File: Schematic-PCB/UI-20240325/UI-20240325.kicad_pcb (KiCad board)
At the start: 2 copper layers, 65.5 x 30.7 mm, 20 parts, among them J1 Conn_01x10_Pin, SW1 SW_Push, SW2 SW_Push, SW3 SW_Push, SW4 SW_Push, SW5 SW_Push

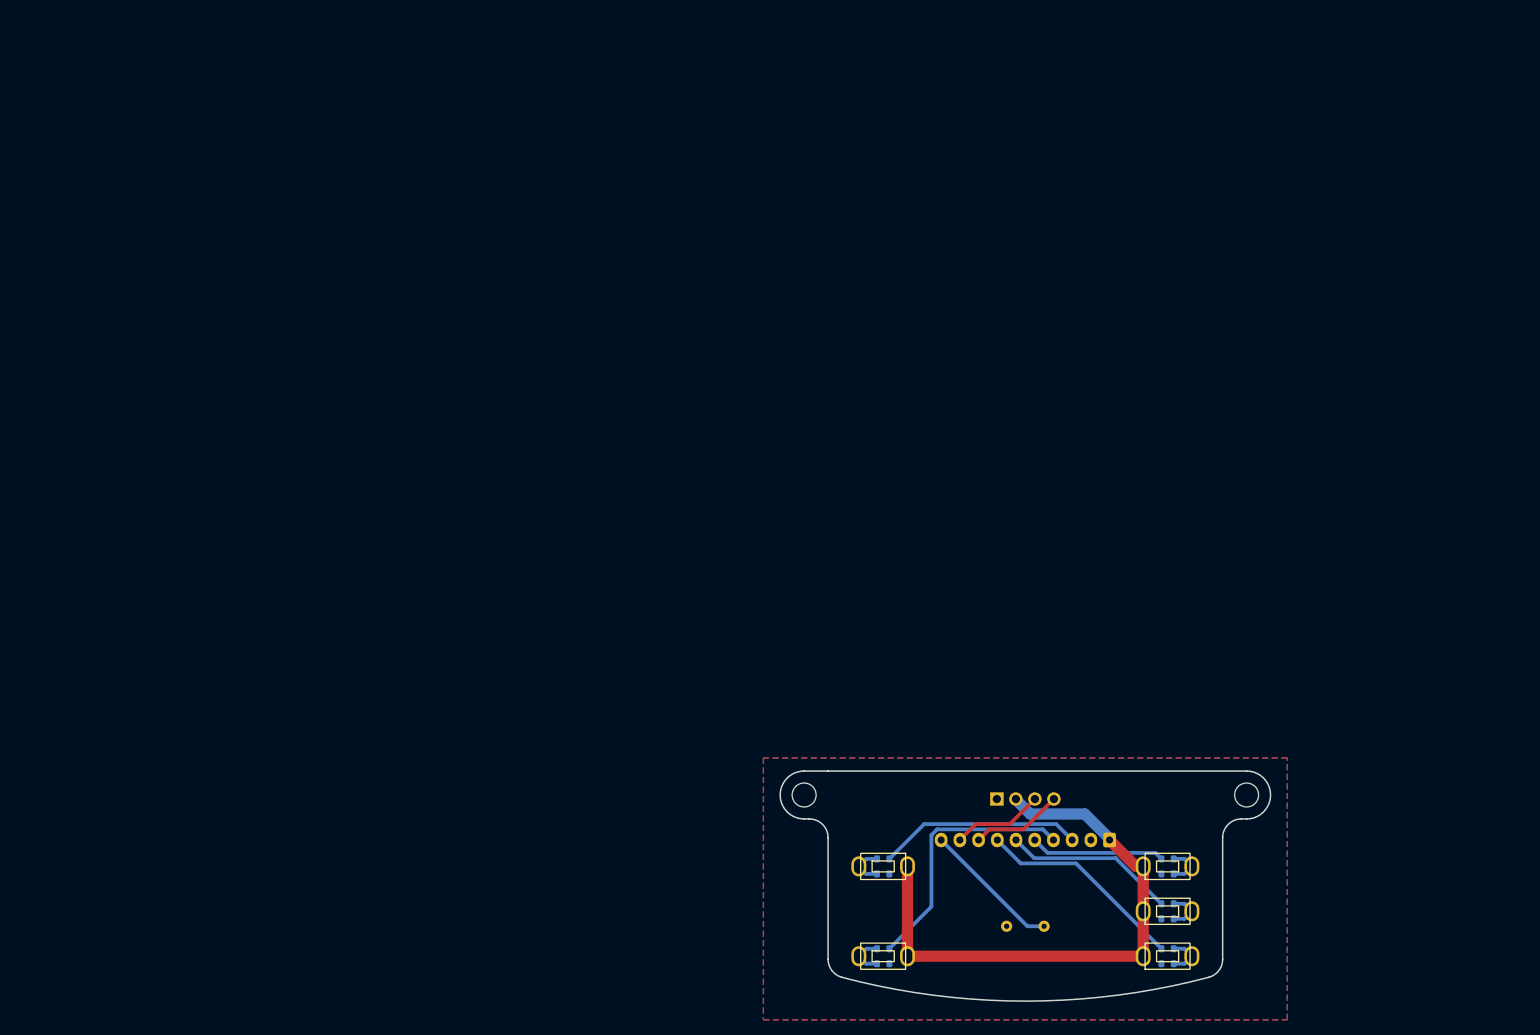
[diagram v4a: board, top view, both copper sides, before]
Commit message: UI基板の配線がねじれてしまう問題を解決した
ピンアサインに変更有、ピンアサイン図の変更が必要
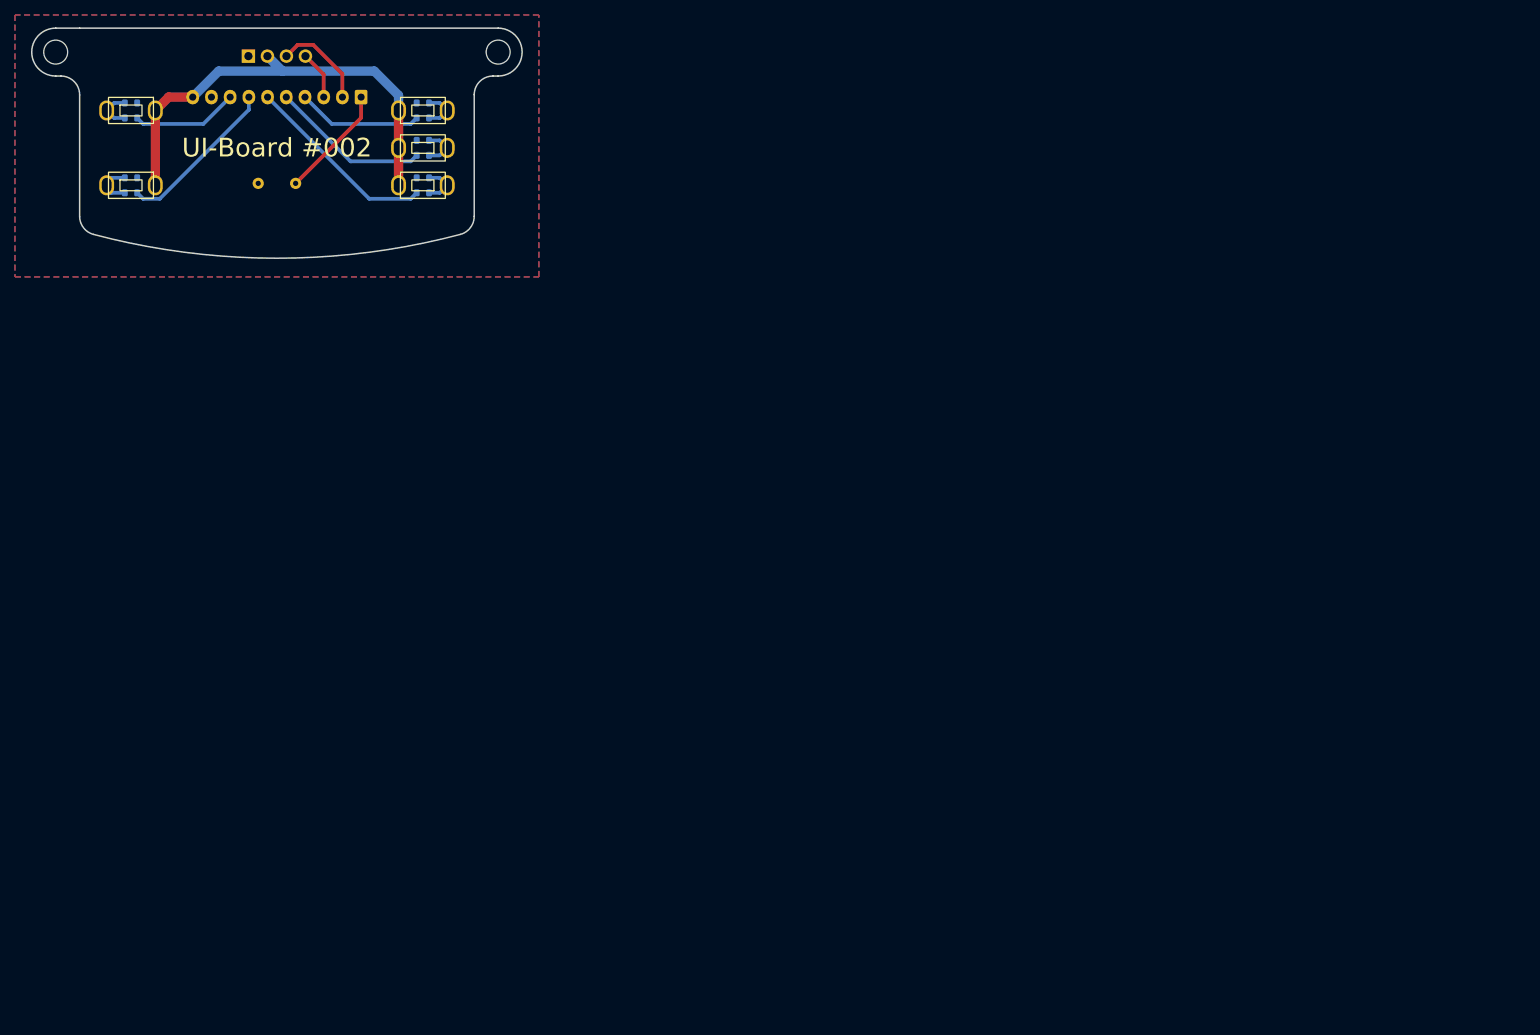
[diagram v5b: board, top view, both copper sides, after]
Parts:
- BZ1: footprint @2024-UI:PKM13EPYH4000-A0 -> @2024TOINIOT2-UI:PKM13EPYH4000-A0
- R5: value 1K -> 500
- SW1, SW2, SW3, SW4, SW5: footprint @2024-UI:TVBP06-B043C -> @2024TOINIOT2-UI:TVBP06-B043C
- U1: footprint @2024-UI:Display -> @2024TOINIOT2-UI:Display
- moved R7 145.3 mm to (-19.5, 20.0)
- moved R10 144.7 mm to (19.5, 20.0)
- moved R9 143.9 mm to (19.5, 15.0)
- moved R6 143.9 mm to (-19.5, 10.0)
- moved SW2 143.9 mm to (-19.5, 21.0)
- moved R8 143.2 mm to (19.5, 10.0)
- moved SW5 143.2 mm to (19.5, 21.0)
- moved SW4 142.5 mm to (19.5, 16.0)
- moved R2 142.5 mm to (-19.5, 22.0)
- moved SW1 142.5 mm to (-19.5, 11.0)
- moved R5 141.8 mm to (19.5, 22.0)
- moved SW3 141.8 mm to (19.5, 11.0)
- moved R1 141.1 mm to (-19.5, 12.0)
- moved R4 141.1 mm to (19.5, 17.0)
- moved REF** 140.9 mm to (29.6, 3.20)
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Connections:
- J1 pad 1: +3.3V -> BUZZER
- J1 pad 10: BUZZER -> +3.3V
- J1 pad 2: GND -> SCL
- J1 pad 3: SW-TAC-1 -> SDA
- J1 pad 4: SW-TAC-2 -> SW-TAC-3
- J1 pad 5: SW-TAC-3 -> SW-TAC-4
- J1 pad 6: SW-TAC-4 -> SW-TAC-5
- J1 pad 7: SW-TAC-5 -> SW-TAC-2
- J1 pad 8: SDA -> SW-TAC-1
- J1 pad 9: SCL -> GND
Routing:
- net +3.3V: track 76.4 -> 60.9 mm
- net SW-TAC-1: track 27.2 -> 14.2 mm
- net SW-TAC-2: track 34.7 -> 21.9 mm
- net SDA: track 12.3 -> 6.49 mm
- net BUZZER: track 18.5 -> 15.1 mm
- net SW-TAC-5: track 27.9 -> 25.9 mm
- net SW-TAC-4: track 23.0 -> 21.3 mm
- net SW-TAC-3: track 18.0 -> 16.7 mm
- net Net-(R2-Pad2): track 5.68 -> 6.48 mm
- net SCL: track 12.3 -> 12.8 mm
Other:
- board text added: "UI-Board #002"

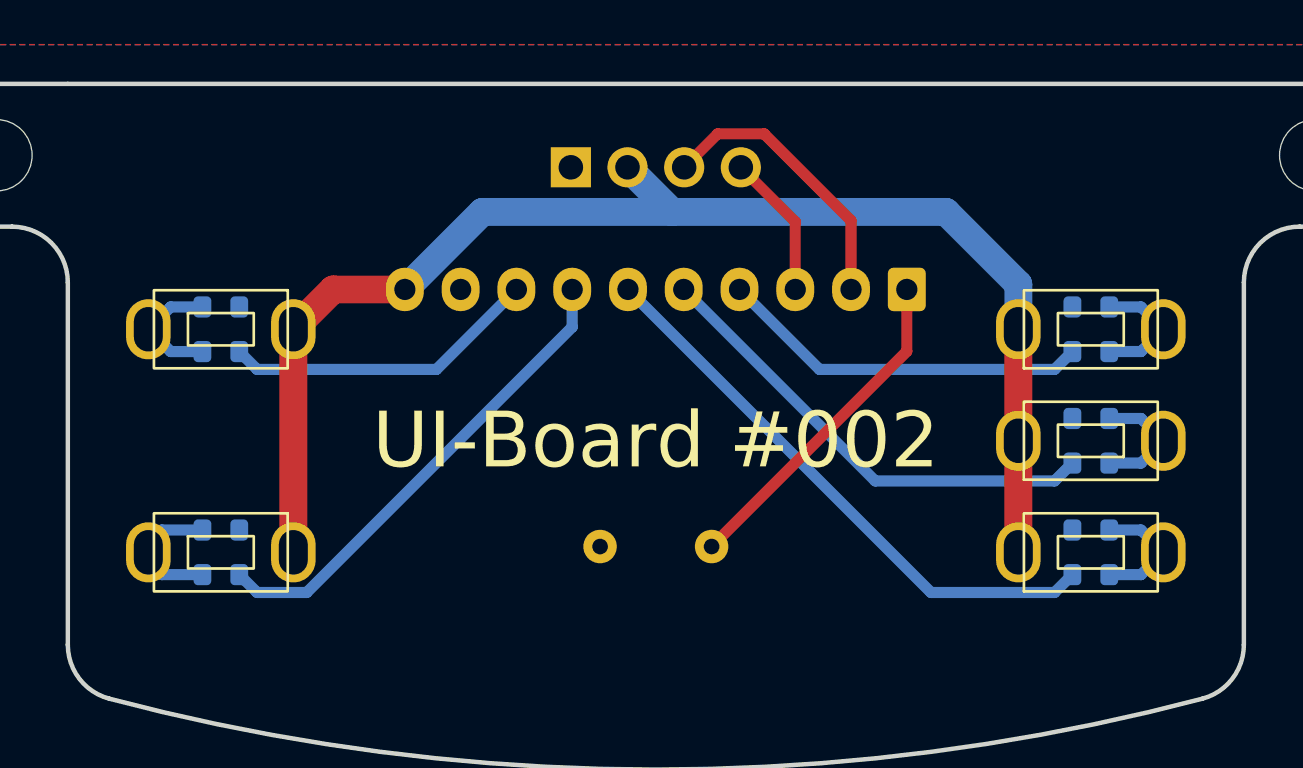
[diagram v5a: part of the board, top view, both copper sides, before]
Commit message: UI基板を修正/MD基板を修正/メイン基板を作り直し （ver.002）
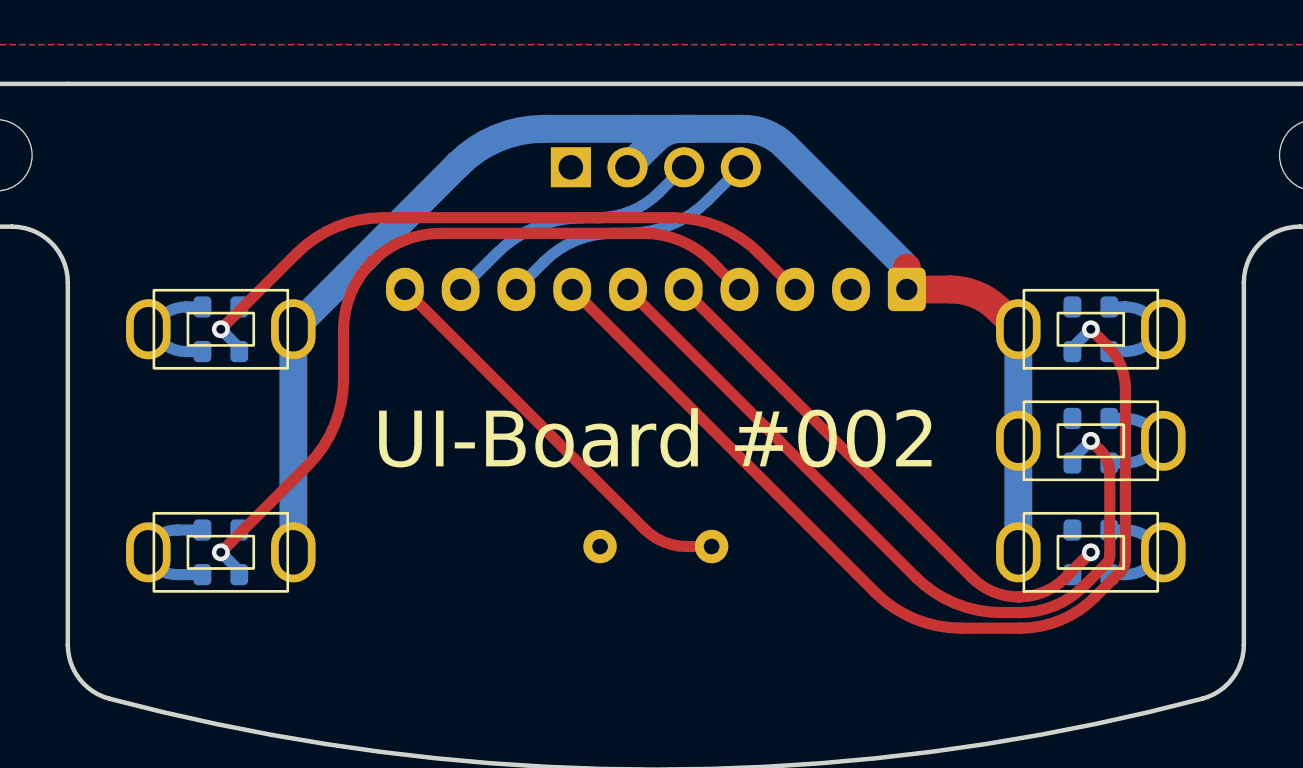
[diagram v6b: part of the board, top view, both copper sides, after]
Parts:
- R1, R2, R3, R4: value 1K -> 500
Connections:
- J1 pad 1: BUZZER -> +3.3V
- J1 pad 10: +3.3V -> BUZZER
- J1 pad 2: SCL -> GND
- J1 pad 3: SDA -> SW-TAC-1
- J1 pad 4: SW-TAC-3 -> SW-TAC-2
- J1 pad 5: SW-TAC-4 -> SW-TAC-5
- J1 pad 6: SW-TAC-5 -> SW-TAC-4
- J1 pad 7: SW-TAC-2 -> SW-TAC-3
- J1 pad 8: SW-TAC-1 -> SDA
- J1 pad 9: GND -> SCL
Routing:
- net SW-TAC-3: track 16.7 -> 44.2 mm, vias 0 -> 1
- net SW-TAC-1: track 14.2 -> 30.0 mm, vias 0 -> 1
- net SW-TAC-4: track 21.3 -> 35.1 mm, vias 0 -> 1
- net SW-TAC-2: track 21.9 -> 34.3 mm, vias 0 -> 1
- net SDA: track 6.49 -> 11.9 mm
- net BUZZER: track 15.1 -> 18.4 mm
- net +3.3V: track 60.9 -> 63.3 mm
- net SCL: track 12.8 -> 11.8 mm
- net SW-TAC-5: track 25.9 -> 25.8 mm, vias 0 -> 1

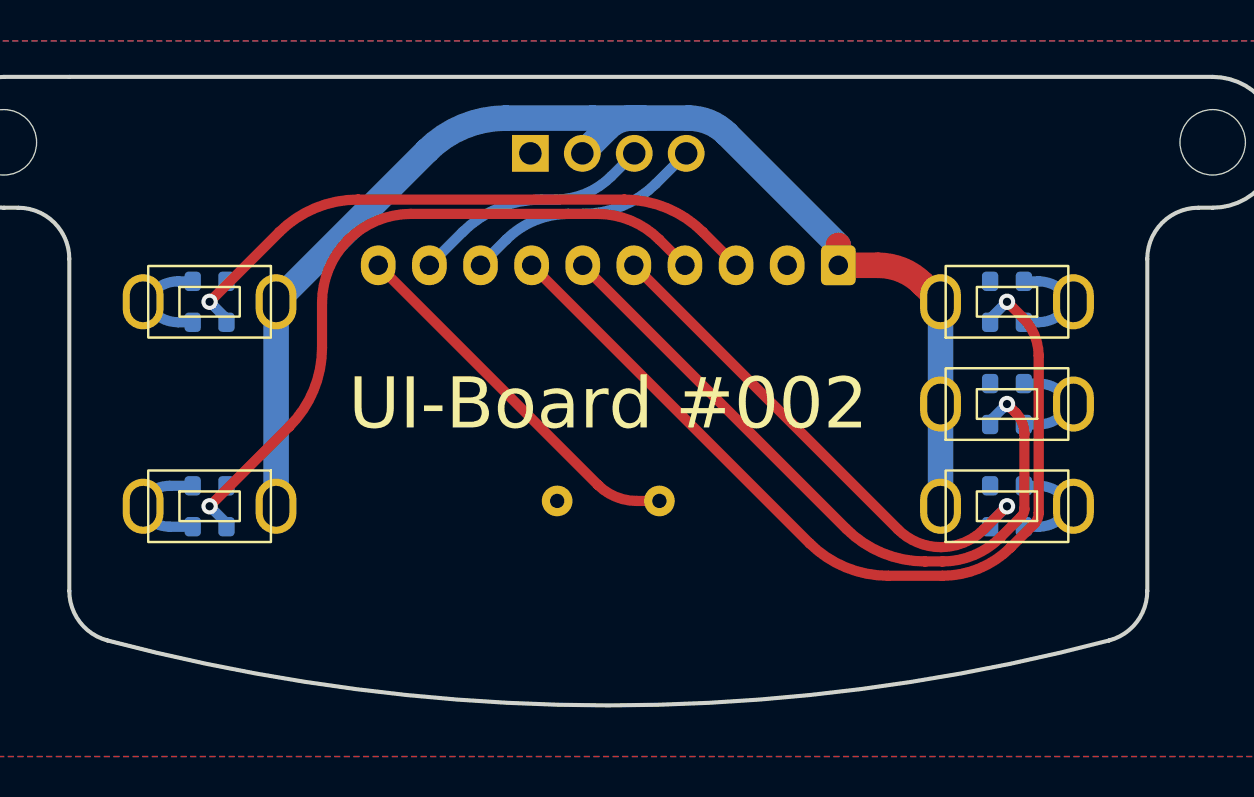
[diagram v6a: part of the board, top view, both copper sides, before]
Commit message: update: UI基板の更新など
発注用ファイルの出力・UI基板の仕様変更
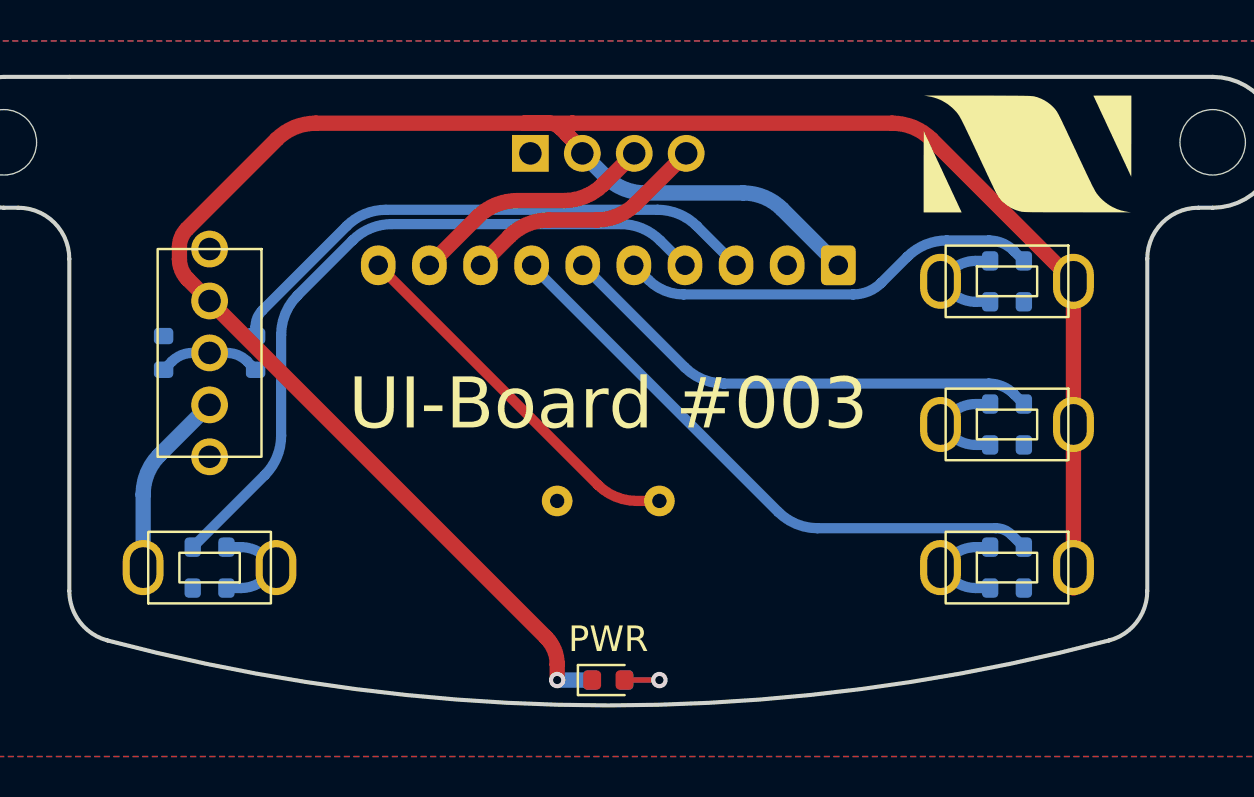
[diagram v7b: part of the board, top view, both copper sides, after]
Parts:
- added D1: PWR, LED_SMD:LED_0603_1608Metric, F.Cu at (0.00, 29.5)
- added R11: 10K, Resistor_SMD:R_0603_1608Metric, B.Cu at (19.5, 25.0)
- J1: value Conn_01x10_Pin -> Conn
- R1, R3, R5: value 500 -> 1K
- R10: value 10K -> 330
- R2, R4: value 500 -> 10K
- R7, R9: value 10K -> 1K
- SW1: value SW_Push -> SW_SPDT; footprint @2024TOINIOT2-UI:TVBP06-B043C -> @2024TOINIOT2-UI:2MS1-T1-B4-VS2-Q-E-S
- moved R3 40.5 mm to (-19.5, 23.0)
- moved R4 39.8 mm to (-19.5, 25.0)
- moved R7 39.2 mm to (19.5, 16.0)
- moved R6 39.0 mm to (19.5, 11.0)
- moved R10 21.7 mm to (0.00, 29.5)
- moved R5 13.0 mm to (19.5, 9.00), turned to 180 degrees
- moved R2 8.79 mm to (-21.8, 13.5), turned to -90 degrees
- moved R8 8.00 mm to (19.5, 18.0), turned to 180 degrees
- moved R9 8.00 mm to (19.5, 23.0), turned to 180 degrees
- moved SW2 3.00 mm to (-19.5, 24.0), turned to 180 degrees
- moved SW5 3.00 mm to (19.5, 24.0), turned to 0 degrees
- moved R1 2.70 mm to (-17.2, 13.5), turned to -90 degrees
- moved SW1 2.50 mm to (-19.5, 13.5), turned to -90 degrees
- moved SW3 1.00 mm to (19.5, 10.0), turned to 0 degrees
- moved SW4 1.00 mm to (19.5, 17.0), turned to 0 degrees
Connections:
- J1 pad 5: SW-TAC-5 -> SW-TAC-3
- J1 pad 7: SW-TAC-3 -> SW-TAC-5
- R1 pad 2: Net-(R1-Pad2) -> Net-(SW1-B)
- R10 pad 1: GND -> +3.3V
- R10 pad 2: Net-(R10-Pad2) -> Net-(D1-A)
- R2 pad 1: SW-TAC-2 -> GND
- R2 pad 2: Net-(R2-Pad2) -> Net-(SW1-B)
- R3 pad 1: SW-TAC-3 -> SW-TAC-2
- R4 pad 1: SW-TAC-4 -> GND
- R4 pad 2: Net-(R4-Pad2) -> Net-(R3-Pad2)
- R5 pad 1: SW-TAC-5 -> SW-TAC-3
- R5 pad 2: Net-(R10-Pad2) -> Net-(R5-Pad2)
- R6 pad 2: Net-(R1-Pad2) -> Net-(R5-Pad2)
- R7 pad 1: GND -> SW-TAC-4
- R7 pad 2: Net-(R2-Pad2) -> Net-(R7-Pad2)
- R8 pad 2: Net-(R3-Pad2) -> Net-(R7-Pad2)
- R9 pad 1: GND -> SW-TAC-5
- R9 pad 2: Net-(R4-Pad2) -> Net-(R11-Pad2)
- SW1 pad 1: Net-(R1-Pad2) -> +3.3V
- SW1 pad 2: +3.3V -> Net-(SW1-B)
- SW2 pad 1: Net-(R2-Pad2) -> Net-(R3-Pad2)
- SW3 pad 1: Net-(R3-Pad2) -> Net-(R5-Pad2)
- SW4 pad 1: Net-(R4-Pad2) -> Net-(R7-Pad2)
- SW5 pad 1: Net-(R10-Pad2) -> Net-(R11-Pad2)
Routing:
- net +3.3V: track 63.3 -> 123.7 mm, vias 0 -> 1
- net SW-TAC-3: track 44.2 -> 20.7 mm, vias 1 -> 0
- net SW-TAC-4: track 35.1 -> 24.2 mm, vias 1 -> 0
- net Net-(R2-Pad2): track 5.98 -> 0.00 mm
- net Net-(R7-Pad2): track 0.00 -> 5.18 mm
- net Net-(R5-Pad2): track 0.00 -> 5.18 mm
- net Net-(R11-Pad2): track 0.00 -> 5.18 mm
- net Net-(R4-Pad2): track 5.18 -> 0.00 mm
- net Net-(R10-Pad2): track 5.18 -> 0.00 mm
- net Net-(R1-Pad2): track 5.18 -> 0.00 mm
- net Net-(SW1-B): track 0.00 -> 5.05 mm
- net SW-TAC-5: track 25.8 -> 29.6 mm, vias 1 -> 0
- net Net-(D1-A): track 0.00 -> 3.39 mm, vias 0 -> 1
- net SW-TAC-1: track 30.0 -> 27.4 mm, vias 1 -> 0
- net SW-TAC-2: track 34.3 -> 35.1 mm, vias 1 -> 0
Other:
- board text added: "PWR"
- board text added: "UI-Board #003"
- board text removed: "UI-Board #002"
